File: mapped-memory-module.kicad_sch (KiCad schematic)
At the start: 10 parts

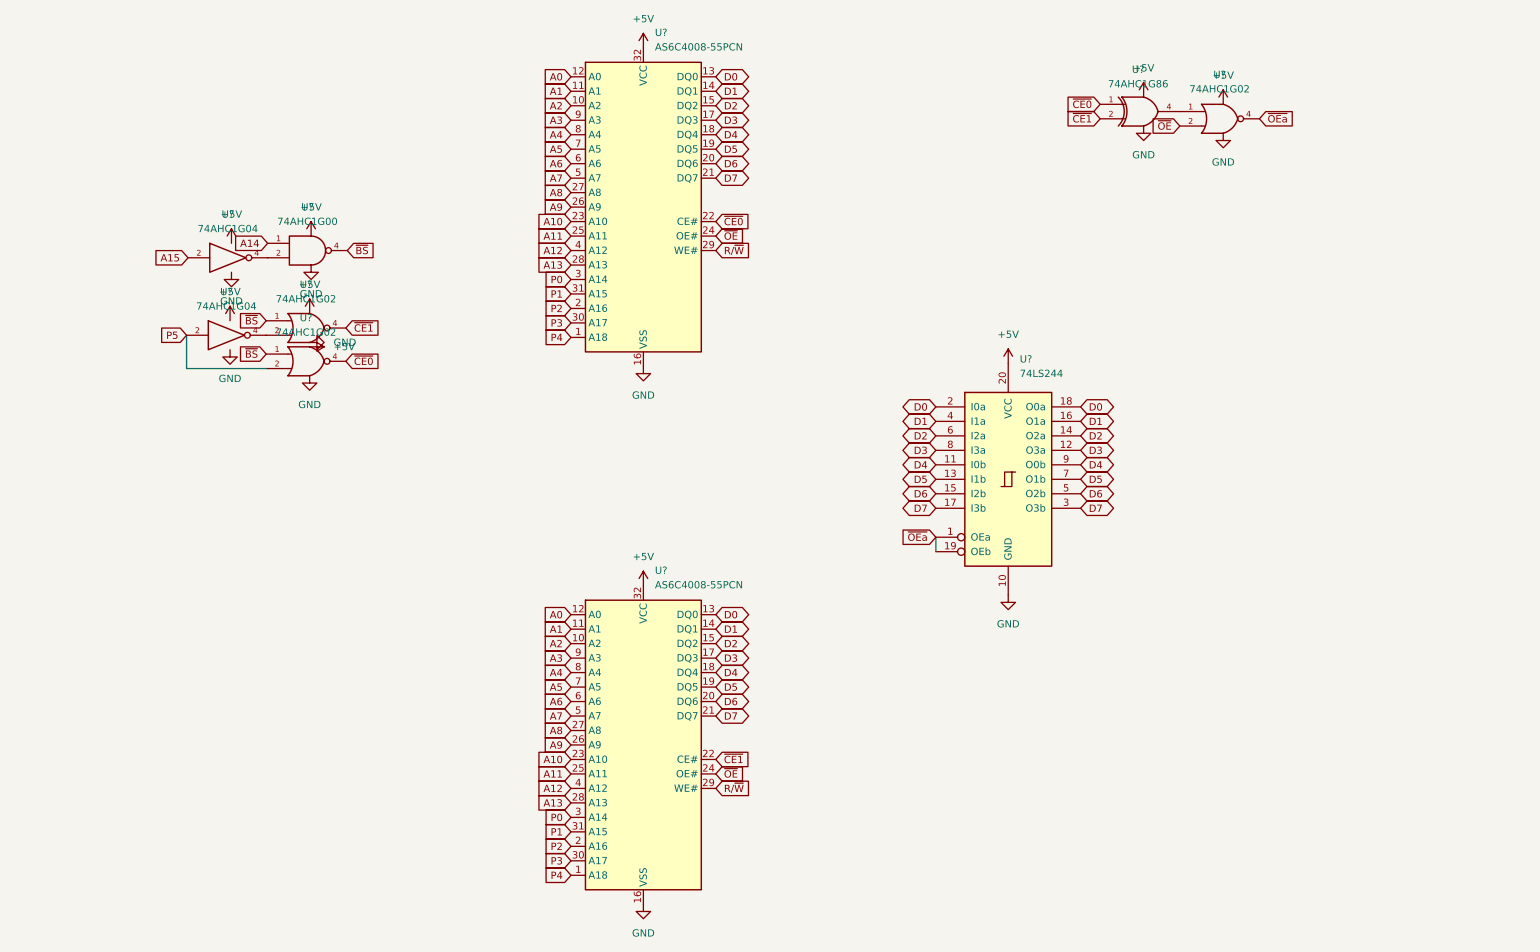
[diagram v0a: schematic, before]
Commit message: fit to sbc design standard
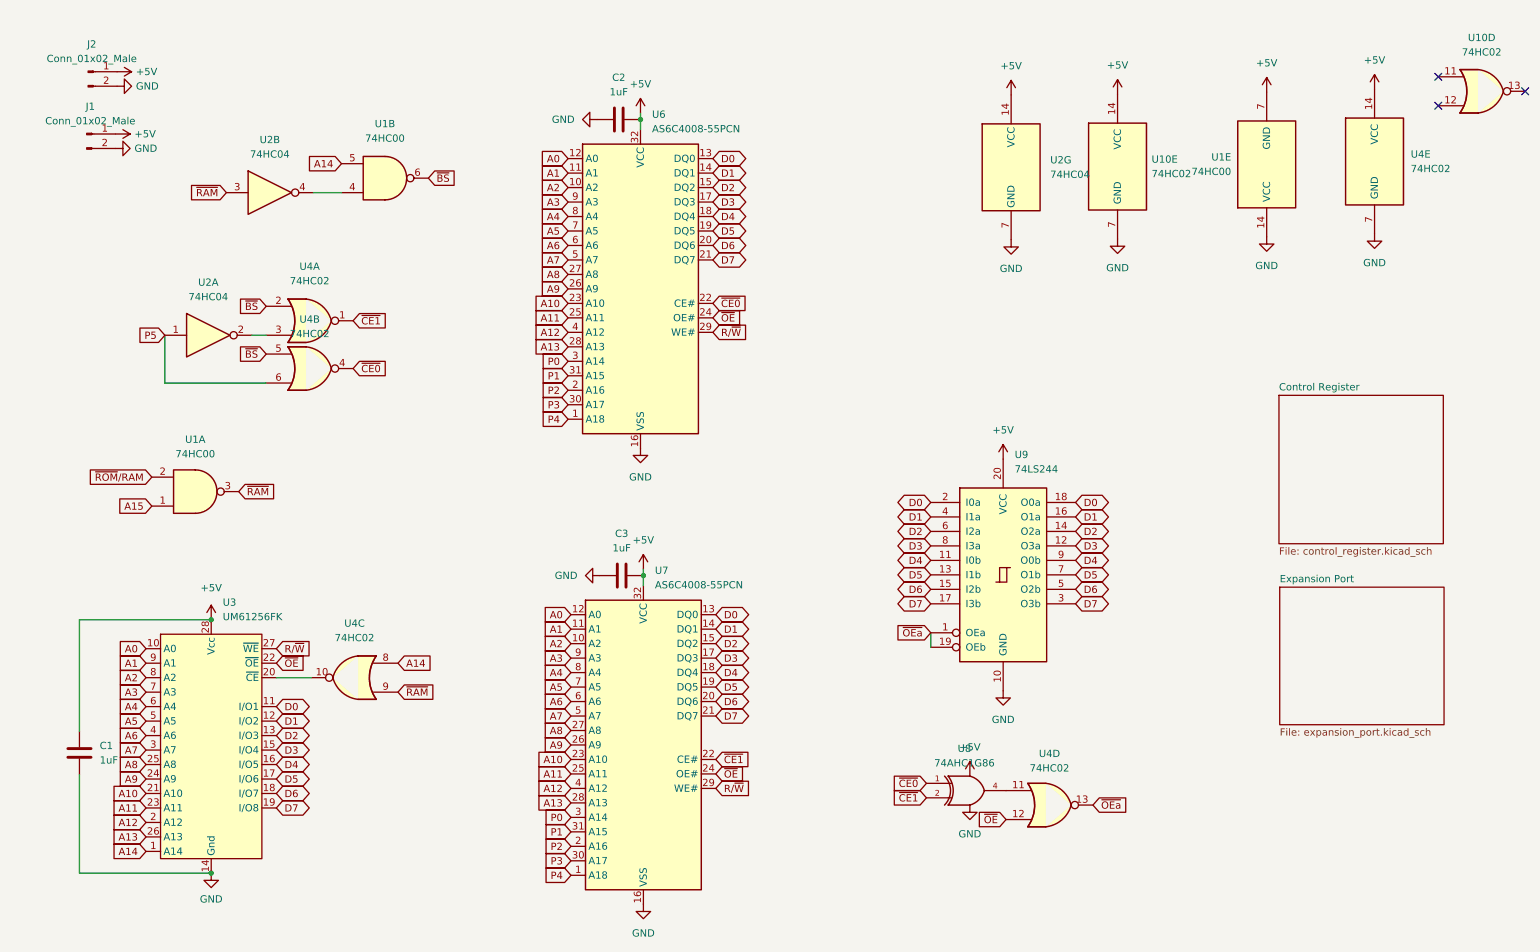
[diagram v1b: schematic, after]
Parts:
- removed U? (x3): 74AHC1G02, symbol 74xGxx:74AHC1G02
- removed U?: 74AHC1G00, symbol 74xGxx:74AHC1G00
- removed U? (x2): 74AHC1G04, symbol 74xGxx:74AHC1G04
- added C1, C2, C3: 1uF, Capacitor_SMD:C_0805_2012Metric, symbol Device:C
- added J1, J2: Conn_01x02_Male, Connector_PinHeader_2.54mm:PinHeader_1x02_P2.54mm_Vertical, symbol Connector:Conn_01x02_Male
- added U1: 74HC00, Package_SO:SO-14_3.9x8.65mm_P1.27mm, symbol 74xx:74HC00
- added U10: 74HC02, Package_SO:SO-14_3.9x8.65mm_P1.27mm, symbol 74xx:74LS02
- added U2: 74HC04, Package_SO:SO-14_3.9x8.65mm_P1.27mm, symbol 74xx:74HC04
- added U3: UM61256FK, Package_DIP:DIP-28_W7.62mm, symbol 6309sbc:UM61256FK
- added U4: 74HC02, Package_SO:SO-14_3.9x8.65mm_P1.27mm, symbol 74xx:74HC02
- U6, U7: renamed from U?; footprint Package_DIP:DIP-32_W15.24mm -> Package_SO:SSOP-32_11.305x20.495mm_P1.27mm
- U8: renamed from U?; footprint (none) -> Package_SO:TSOP-5_1.65x3.05mm_P0.95mm
- U9: renamed from U?; footprint (none) -> Package_SO:SO-20_5.3x12.6mm_P1.27mm
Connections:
- net +5V: now also C1.1, C2.1, C3.1, J1.1 (Pin_1), J2.1 (Pin_1), U1.7 (GND), U10.14 (VCC), U2.14 (VCC), U3.28 (Vcc), U4.14 (VCC)
- net A0: now also U3.10 (A0)
- net A1: now also U3.9 (A1)
- net A10: now also U3.21 (A10)
- net A11: now also U3.23 (A11)
- net A12: now also U3.2 (A12)
- net A13: now also U3.26 (A13)
- net A14: now also U1.5, U3.1 (A14), U4.8
- net A15: now also U1.1
- net A2: now also U3.8 (A2)
- net A3: now also U3.7 (A3)
- net A4: now also U3.6 (A4)
- net A5: now also U3.5 (A5)
- net A6: now also U3.4 (A6)
- net A7: now also U3.3 (A7)
- net A8: now also U3.25 (A8)
- net A9: now also U3.24 (A9)
- net D0: now also U3.11 (I/O1)
- net D1: now also U3.12 (I/O2)
- net D2: now also U3.13 (I/O3)
- net D3: now also U3.15 (I/O4)
- net D4: now also U3.16 (I/O5)
- net D5: now also U3.17 (I/O6)
- net D6: now also U3.18 (I/O7)
- net D7: now also U3.19 (I/O8)
- net GND: now also C1.2, C2.2, C3.2, J1.2 (Pin_2), J2.2 (Pin_2), U1.14 (VCC), U10.7 (GND), U2.7 (GND), U3.14 (Gnd), U4.7 (GND)
- net P5: now also U2.1, U4.6
- net R/~{W}: now also U3.27 (~{WE})
- net ~{BS}: now also U1.6, U4.2, U4.5
- net ~{CE0}: now also U4.4
- net ~{CE1}: now also U4.1
- net ~{OEa}: now also U4.13
- net ~{OE}: now also U3.22 (~{OE}), U4.12
- net at U8.4: now also U4.11
- new net: U3.20 (~{CE}), U4.10
- new net: U2.2, U4.3
- new net: U1.4, U2.4
- new net ~{RAM}: U1.3, U2.3, U4.9
- new net ~{ROM}/RAM: U1.2
- no-connect marks 0 -> 3
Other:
- added sheet Control Register (control_register.kicad_sch)
- added sheet Expansion Port (expansion_port.kicad_sch)
- moved on the sheet: U6, U8, U9

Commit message: add mapped memory lane
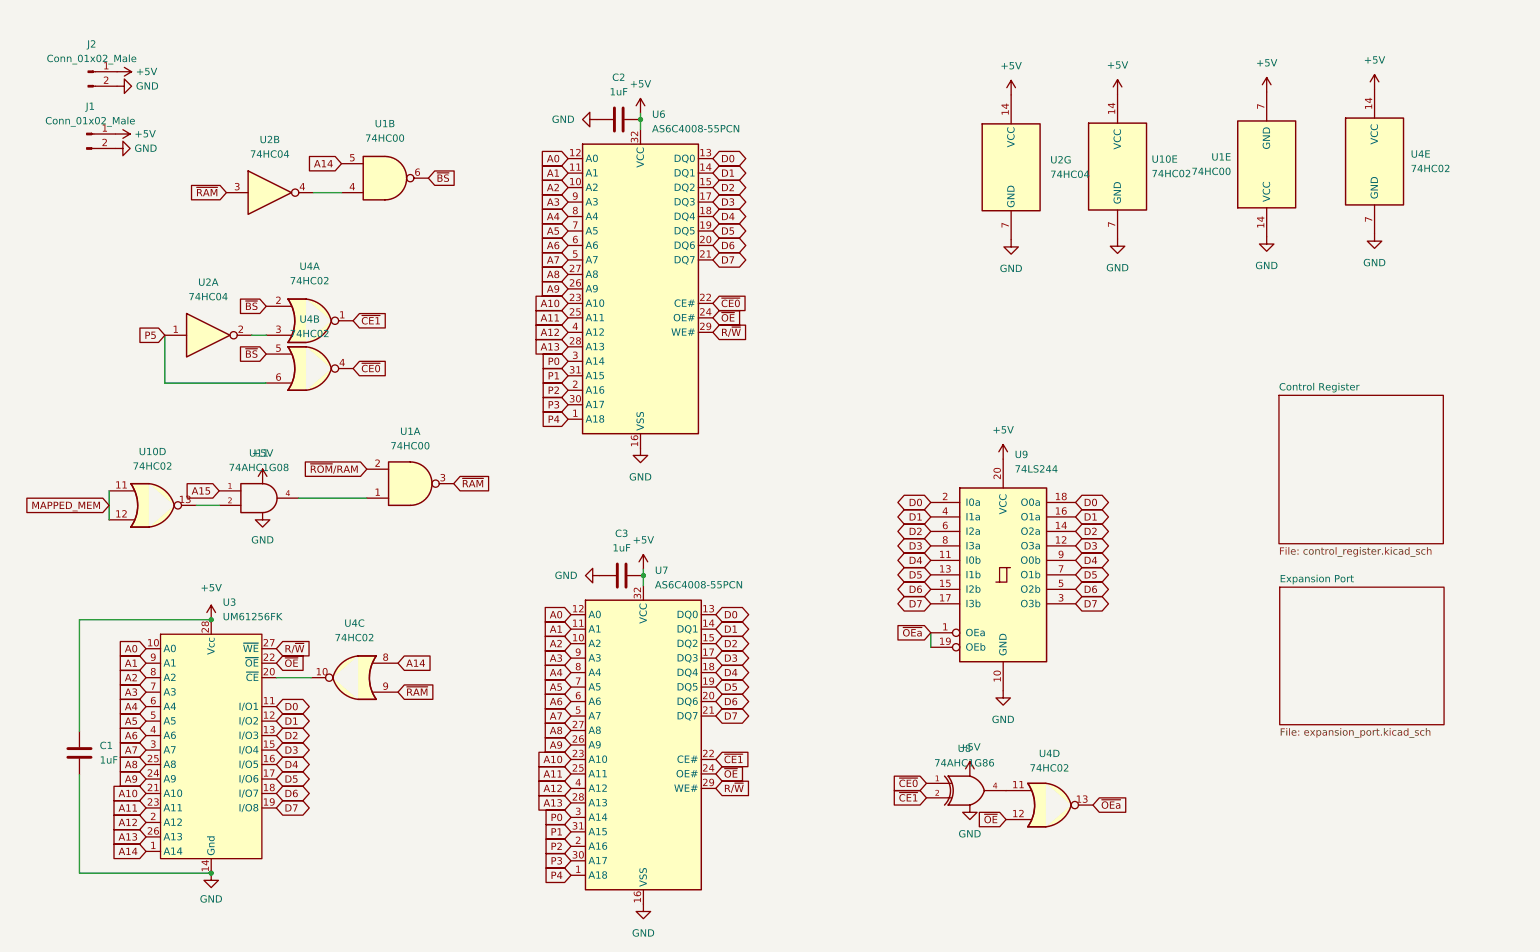
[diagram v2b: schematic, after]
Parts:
- added U11: 74AHC1G08, Package_SO:TSOP-5_1.65x3.05mm_P0.95mm, symbol 74xGxx:74AHC1G08
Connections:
- net +5V: now also U11.5 (VCC)
- net A15: now also U11.1; no longer U1.1
- net GND: now also U11.3 (GND)
- net MAPPED_MEM: now reaches U10.11
- net MAPPED_MEM: now also U10.12
- net at U10.13: now also U11.2
- new net: U1.1, U11.4
- no-connect marks 3 -> 0
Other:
- moved on the sheet: U10D, U1A
